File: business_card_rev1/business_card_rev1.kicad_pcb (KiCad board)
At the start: 2 copper layers, 0 parts

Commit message: Chose components and drafted rough PCB layout.
Need to check schematic and clean up layout.
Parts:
- added B1: BAT-HLD-012-SMT, BAT_HLD_012_SMT:BAT-HLD-012-SMT_TEC, F.Cu at (147.4, 74.0)
- added C1: 4.3pF, Capacitor_SMD:C_0402_1005Metric, F.Cu at (103.2, 68.4)
- added C11: 100n, Capacitor_SMD:C_0402_1005Metric, F.Cu at (113.4, 75.1)
- added C12: 100n, Capacitor_SMD:C_0402_1005Metric, F.Cu at (103.6, 74.7)
- added C2: 4.3pF, Capacitor_SMD:C_0402_1005Metric, F.Cu at (101.5, 72.5)
- added C3: 110nF, Capacitor_SMD:C_0402_1005Metric, F.Cu at (93.0, 81.6)
- added C6: 100n, Capacitor_SMD:C_0402_1005Metric, F.Cu at (99.3, 75.5)
- added C7: 100nF, Capacitor_SMD:C_0402_1005Metric, F.Cu at (167.1, 78.5)
- added C8: 100n, Capacitor_SMD:C_0402_1005Metric, F.Cu at (114.7, 75.1)
- added C9: 100n, Capacitor_SMD:C_0402_1005Metric, F.Cu at (116.0, 75.1)
- added D1: Green LED, LED_SMD:LED_0805_2012Metric, F.Cu at (166.6, 73.0)
- added D2: LED, Resistor_SMD:R_0603_1608Metric, F.Cu at (127.3, 85.4)
- added D3: LED, Resistor_SMD:R_0603_1608Metric, F.Cu at (124.8, 85.4)
- added D4: LED, Resistor_SMD:R_0603_1608Metric, F.Cu at (122.3, 85.4)
- added D5: LED, Resistor_SMD:R_0603_1608Metric, F.Cu at (119.8, 85.4)
- added D6: LED, Resistor_SMD:R_0603_1608Metric, F.Cu at (117.3, 85.4)
- added D7: LED, Resistor_SMD:R_0603_1608Metric, F.Cu at (114.8, 85.4)
- added D8: LED, Resistor_SMD:R_0603_1608Metric, F.Cu at (112.3, 85.4)
- added D9: LED, Resistor_SMD:R_0603_1608Metric, F.Cu at (109.8, 85.4)
- added FB1: FerriteBead_Small, Resistor_SMD:R_0603_1608Metric, F.Cu at (101.0, 76.9)
- added J1: Conn_02x05_Counter_Clockwise, Connector_PinHeader_1.00mm:PinHeader_2x05_P1.00mm_Vertical, F.Cu at (91.0, 68.6)
- added J2: Conn_01x03_Pin, Connector_PinHeader_1.00mm:PinHeader_1x03_P1.00mm_Vertical, F.Cu at (91.2, 77.0)
- added R1: 10k, Resistor_SMD:R_0603_1608Metric, F.Cu at (108.3, 68.5)
- added R10: 75, Resistor_SMD:R_0603_1608Metric, F.Cu at (114.7, 88.9)
- added R11: 75, Resistor_SMD:R_0603_1608Metric, F.Cu at (117.3, 88.9)
- added R12: 75, Resistor_SMD:R_0603_1608Metric, F.Cu at (119.8, 88.7)
- added R13: 75, Resistor_SMD:R_0603_1608Metric, F.Cu at (122.3, 88.7)
- added R14: 75, Resistor_SMD:R_0603_1608Metric, F.Cu at (124.9, 88.7)
- added R15: 75, Resistor_SMD:R_0603_1608Metric, F.Cu at (127.4, 88.9)
- added R16: 20R, Resistor_SMD:R_0402_1005Metric, F.Cu at (113.9, 72.8)
- added R17: 20R, Resistor_SMD:R_0402_1005Metric, F.Cu at (103.6, 77.8)
- added R18: 20R, Resistor_SMD:R_0402_1005Metric, F.Cu at (103.6, 76.6)
- added R2: 100, Resistor_SMD:R_0603_1608Metric, F.Cu at (91.4, 74.8)
- added R3: 75R, Resistor_SMD:R_0603_1608Metric, F.Cu at (170.2, 72.7)
- added R4: 75, Resistor_SMD:R_0603_1608Metric, F.Cu at (109.8, 89.0)
- added R8: 20R, Resistor_SMD:R_0402_1005Metric, F.Cu at (112.0, 70.5)
- added R9: 75, Resistor_SMD:R_0603_1608Metric, F.Cu at (112.3, 89.0)
- added U1: STM32L031F6P6, STM32L031F6P6:TSSOP20, F.Cu at (108.7, 75.1)
- added U2: LD39015M33R, Package_TO_SOT_SMD:SOT-23-5, F.Cu at (170.0, 78.1)
- added U3: PTS645SM43SMTR92LFS, PTS645SM43SMTR92LFS:SWITCH_43SMTR92LFS, F.Cu at (92.9, 87.4)
- added X1: MU00525-32.768K, MU00525_32_768K:XTAL_MU00525_NDK, F.Cu at (103.4, 71.5)
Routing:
- net VDD: track 0.00 -> 145.4 mm
- net NRST: track 0.00 -> 75.2 mm
- net VBAT: track 0.00 -> 55.5 mm
- net GND: track 0.00 -> 46.1 mm, vias 0 -> 12
- net /MCU/SWDIO: track 0.00 -> 30.5 mm
- net /MCU/SWCLK: track 0.00 -> 28.2 mm
- net /MCU/OSC32_IN: track 0.00 -> 24.2 mm
- net MSG_BIT7: track 0.00 -> 20.7 mm
- net MSG_BIT6: track 0.00 -> 20.3 mm
- net MSG_BIT5: track 0.00 -> 18.7 mm
- net /MCU/USART2_TX: track 0.00 -> 14.2 mm
- net /MCU/USART2_RX: track 0.00 -> 13.8 mm
- net MSG_BIT1: track 0.00 -> 12.3 mm
- net MSG_BIT4: track 0.00 -> 12.0 mm
- net MSG_BIT0: track 0.00 -> 11.2 mm
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- added copper zone on B.Cu, net GND
- added copper zone on F.Cu, net GND
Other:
- board outline added: 86 x 54 mm
- board text added: "Ihsan Salari"
- board text added: "University of Waterloo"

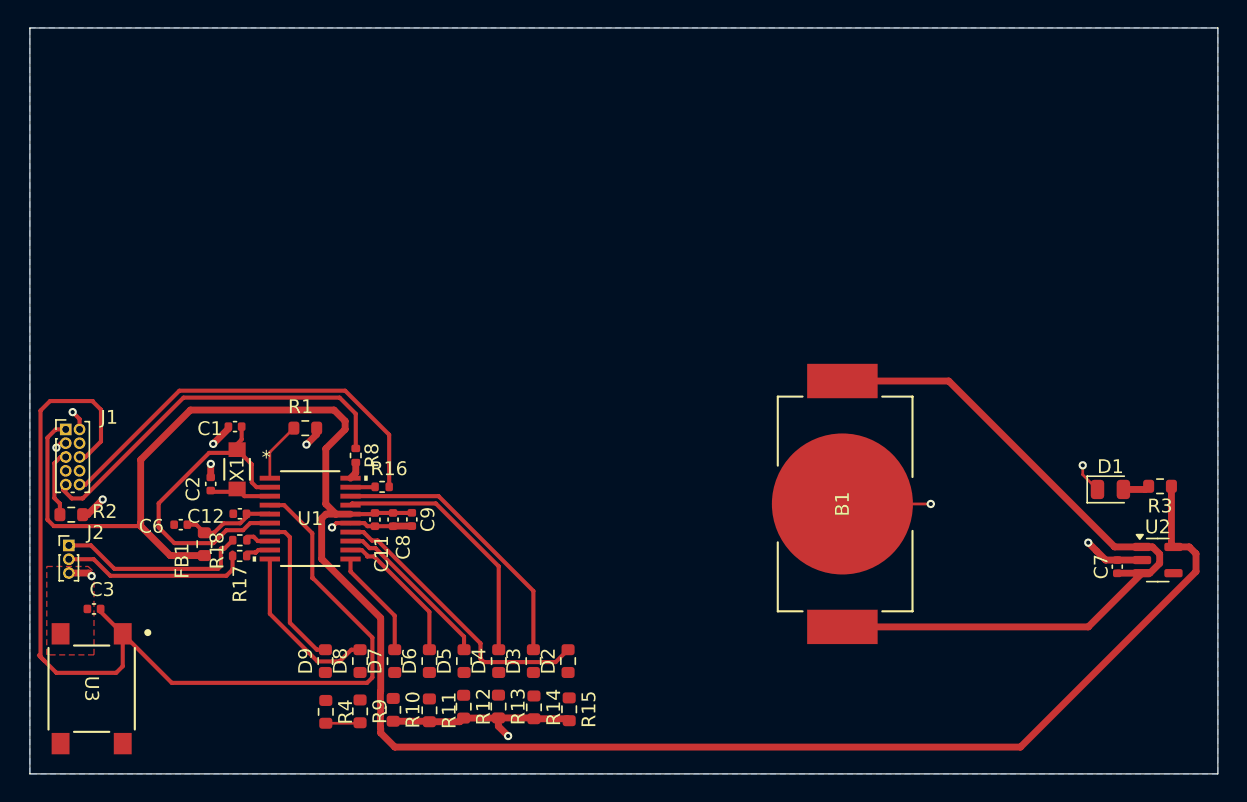
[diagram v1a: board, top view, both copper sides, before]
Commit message: Completed layout V1.
Need to review schematic and layout and verify component selection.
Need to add silkscreen info.
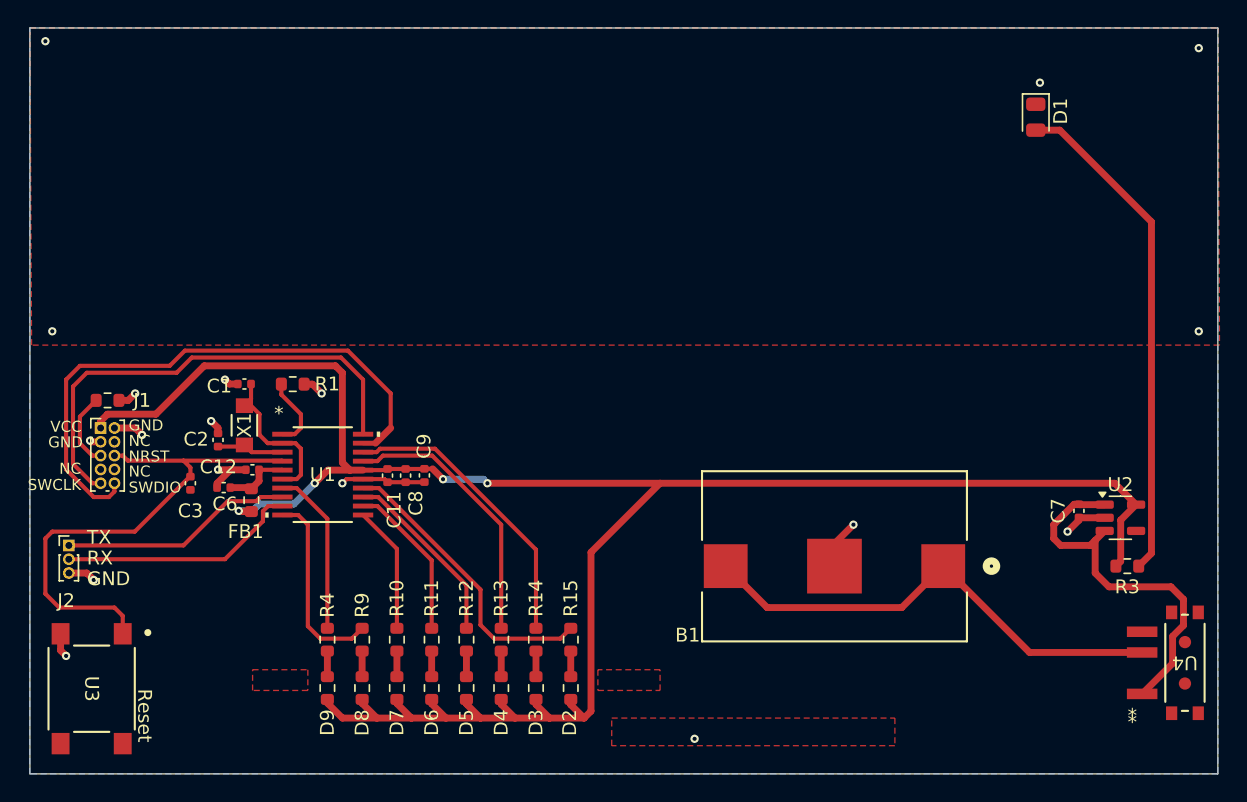
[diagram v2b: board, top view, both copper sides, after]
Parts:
- removed R16, R17, R18, R8: 20R, Resistor_SMD:R_0402_1005Metric
- added U4: PCM12SMTR, PCM12SMTR:PCM12SMTR_CNK, F.Cu at (172.0, 85.5)
- B1: value BAT-HLD-012-SMT -> 3000; footprint BAT_HLD_012_SMT:BAT-HLD-012-SMT_TEC -> keystone3000batholder:3000_KEY
- moved D1 27.5 mm to (161.2, 46.0), turned to -90 degrees
- moved C3 11.5 mm to (100.0, 72.5), turned to -90 degrees
- moved R2 8.68 mm to (94.0, 66.5)
- moved R3 6.25 mm to (167.8, 78.5), turned to 0 degrees
- moved R4 5.23 mm to (109.9, 83.8), turned to 90 degrees
- moved R9 5.19 mm to (112.4, 83.8), turned to 90 degrees
- moved R11 5.12 mm to (117.5, 83.8), turned to 90 degrees
- moved R10 5.09 mm to (114.9, 83.8), turned to 90 degrees
- moved R15 5.04 mm to (127.5, 83.8), turned to 90 degrees
- moved R14 4.90 mm to (125.0, 83.8), turned to 90 degrees
- moved C7 4.90 mm to (164.3, 74.5), turned to -90 degrees
- moved R12 4.85 mm to (120.0, 83.8), turned to 90 degrees
- moved R13 4.84 mm to (122.5, 83.8), turned to 90 degrees
- moved FB1 4.66 mm to (104.4, 73.7)
- moved C6 4.11 mm to (102.4, 72.8)
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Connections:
- B1 pad 1: VBAT -> Net-(B1-Pad1)
- B1 pad 2: VBAT -> Net-(B1-Pad1)
- D2 pad 2: MSG_BIT7 -> VDD
- D3 pad 2: MSG_BIT6 -> VDD
- D4 pad 2: MSG_BIT5 -> VDD
- D5 pad 2: MSG_BIT4 -> VDD
- D6 pad 2: MSG_BIT3 -> VDD
- D7 pad 2: MSG_BIT2 -> VDD
- D8 pad 2: MSG_BIT1 -> VDD
- D9 pad 2: MSG_BIT0 -> VDD
- R10 pad 2: GND -> MSG_BIT2
- R11 pad 2: GND -> MSG_BIT3
- R12 pad 2: GND -> MSG_BIT4
- R13 pad 2: GND -> MSG_BIT5
- R14 pad 2: GND -> MSG_BIT6
- R15 pad 2: GND -> MSG_BIT7
- R4 pad 2: GND -> MSG_BIT0
- R9 pad 2: GND -> MSG_BIT1
- U1 pad 19: Net-(U1-PA13) -> /MCU/SWDIO
- U1 pad 20: Net-(U1-PA14) -> /MCU/SWCLK
- U1 pad 8: Net-(U1-PA2) -> /MCU/USART2_TX
- U1 pad 9: Net-(U1-PA3) -> /MCU/USART2_RX
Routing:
- net NRST: track 75.2 -> 37.6 mm
- net Net-(B1-Pad1): track 0.00 -> 35.2 mm
- net Net-(D1-A): track 1.92 -> 36.4 mm
- net VBAT: track 55.5 -> 27.3 mm
- net GND: track 46.1 -> 28.5 mm, vias 12 -> 18
- net /MCU/OSC32_IN: track 24.2 -> 11.4 mm
- net /MCU/SWDIO: track 30.5 -> 42.2 mm
- net /MCU/SWCLK: track 28.2 -> 34.7 mm
- net VDD: track 145.4 -> 151.4 mm, vias 0 -> 4
- net /MCU/USART2_RX: track 13.8 -> 17.5 mm
- net /MCU/USART2_TX: track 14.2 -> 16.9 mm
- net VDDA: track 7.05 -> 4.86 mm
- net Net-(D9-K): track 0.00 -> 1.85 mm
- net Net-(D8-K): track 0.00 -> 1.85 mm
- net Net-(D7-K): track 0.00 -> 1.85 mm
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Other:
- board text added: "BIT 0"
- board text added: "BIT 7"
- board text added: "Decode the ASCII message"
- board text added: "GND"
- board text added: "NC"
- board text added: "NRST"
- board text added: "RX"
- board text added: "Reset"
- board text added: "SWCLK"
- board text added: "SWDIO"
- board text added: "TX"
- board text added: "VCC"

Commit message: [HW] Edits to PCB design and added QR codes.
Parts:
- removed C7: 100nF, Capacitor_SMD:C_0402_1005Metric
- removed J1: Conn_02x05_Counter_Clockwise, Connector_PinHeader_1.00mm:PinHeader_2x05_P1.00mm_Vertical
- removed R2: 100, Resistor_SMD:R_0603_1608Metric
- removed U2: LD39015M33R, Package_TO_SOT_SMD:SOT-23-5
- added C13: 100n, Capacitor_SMD:C_0402_1005Metric, F.Cu at (118.0, 73.5)
- added J3: Conn_01x05_Pin, Connector_PinHeader_1.00mm:PinHeader_1x05_P1.00mm_Vertical, F.Cu at (91.0, 70.5)
- added R5: 10k, Resistor_SMD:R_0603_1608Metric, F.Cu at (98.5, 76.0)
- C11, C8: value 100n -> 1u
- C3: value 110nF -> 100n
- R10, R11, R12, R13, R14, R15, R4, R9: value 75 -> 250
- moved C1 3.81 mm to (105.0, 69.0), turned to 90 degrees
- moved C2 3.36 mm to (105.0, 70.9), turned to -90 degrees
- moved FB1 2.91 mm to (101.5, 73.8)
- moved X1 2.07 mm to (102.7, 70.0)
- moved R3 1.95 mm to (168.5, 80.3), turned to 90 degrees
- moved C6 1.57 mm to (103.9, 73.3), turned to -90 degrees
- moved C12 1.42 mm to (105.0, 72.8), turned to -90 degrees
- moved D1 0.50 mm to (161.2, 45.5), turned to 90 degrees
- moved J2 0.20 mm to (91.0, 77.0)
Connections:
- net NRST renamed /MCU/NRST
- U4 pad 1: VBAT -> VDD
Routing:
- net VBAT: track 27.3 -> 0.00 mm
- net GND: track 28.5 -> 18.5 mm, vias 18 -> 11
- net VDD: track 151.4 -> 160.8 mm
- net Net-(J1-Pin_5): track 5.46 -> 0.00 mm
- net /MCU/SWDIO: track 42.2 -> 38.1 mm, vias 0 -> 1
- net /MCU/NRST: track 37.6 -> 41.4 mm, vias 0 -> 2
- net Net-(D1-A): track 36.4 -> 39.3 mm
- net MSG_BIT6: track 21.3 -> 23.4 mm
- net VDDA: track 4.86 -> 6.38 mm
- net MSG_BIT5: track 19.7 -> 20.6 mm
- net /MCU/SWCLK: track 34.7 -> 33.8 mm
- net /MCU/OSC32_IN: track 11.4 -> 12.2 mm
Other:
- board text added: "GitHub"
- board text added: "LinkedIn"
- board text added: "isalari@uwaterloo.ca"
- board text removed: "NC"

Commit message: Final changes. PCB ordered.
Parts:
- U3: footprint PTS645SM43SMTR92LFS:SWITCH_43SMTR92LFS -> 5mm pushbutton2:SW4_1437565_TEC
- U4: footprint PCM12SMTR:PCM12SMTR_CNK -> K3-1296S-E2:K31296SE2
- moved R3 4.83 mm to (168.5, 75.5)
- moved U4 1.00 mm to (172.0, 86.5), turned to -90 degrees
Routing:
- net Net-(D1-A): track 39.3 -> 34.5 mm
- net VDD: track 160.8 -> 162.9 mm, vias 4 -> 6
- net Net-(B1-Pad1): track 35.2 -> 36.7 mm
- net GND: track 18.5 -> 18.7 mm, vias 11 -> 12
